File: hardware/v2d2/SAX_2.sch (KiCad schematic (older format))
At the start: 80 parts, among them J1 Prog port, J2 SSD1306, U1 74HC165, U2 74HC165, U3 74HC165, U4 BluePill_STM32F103C

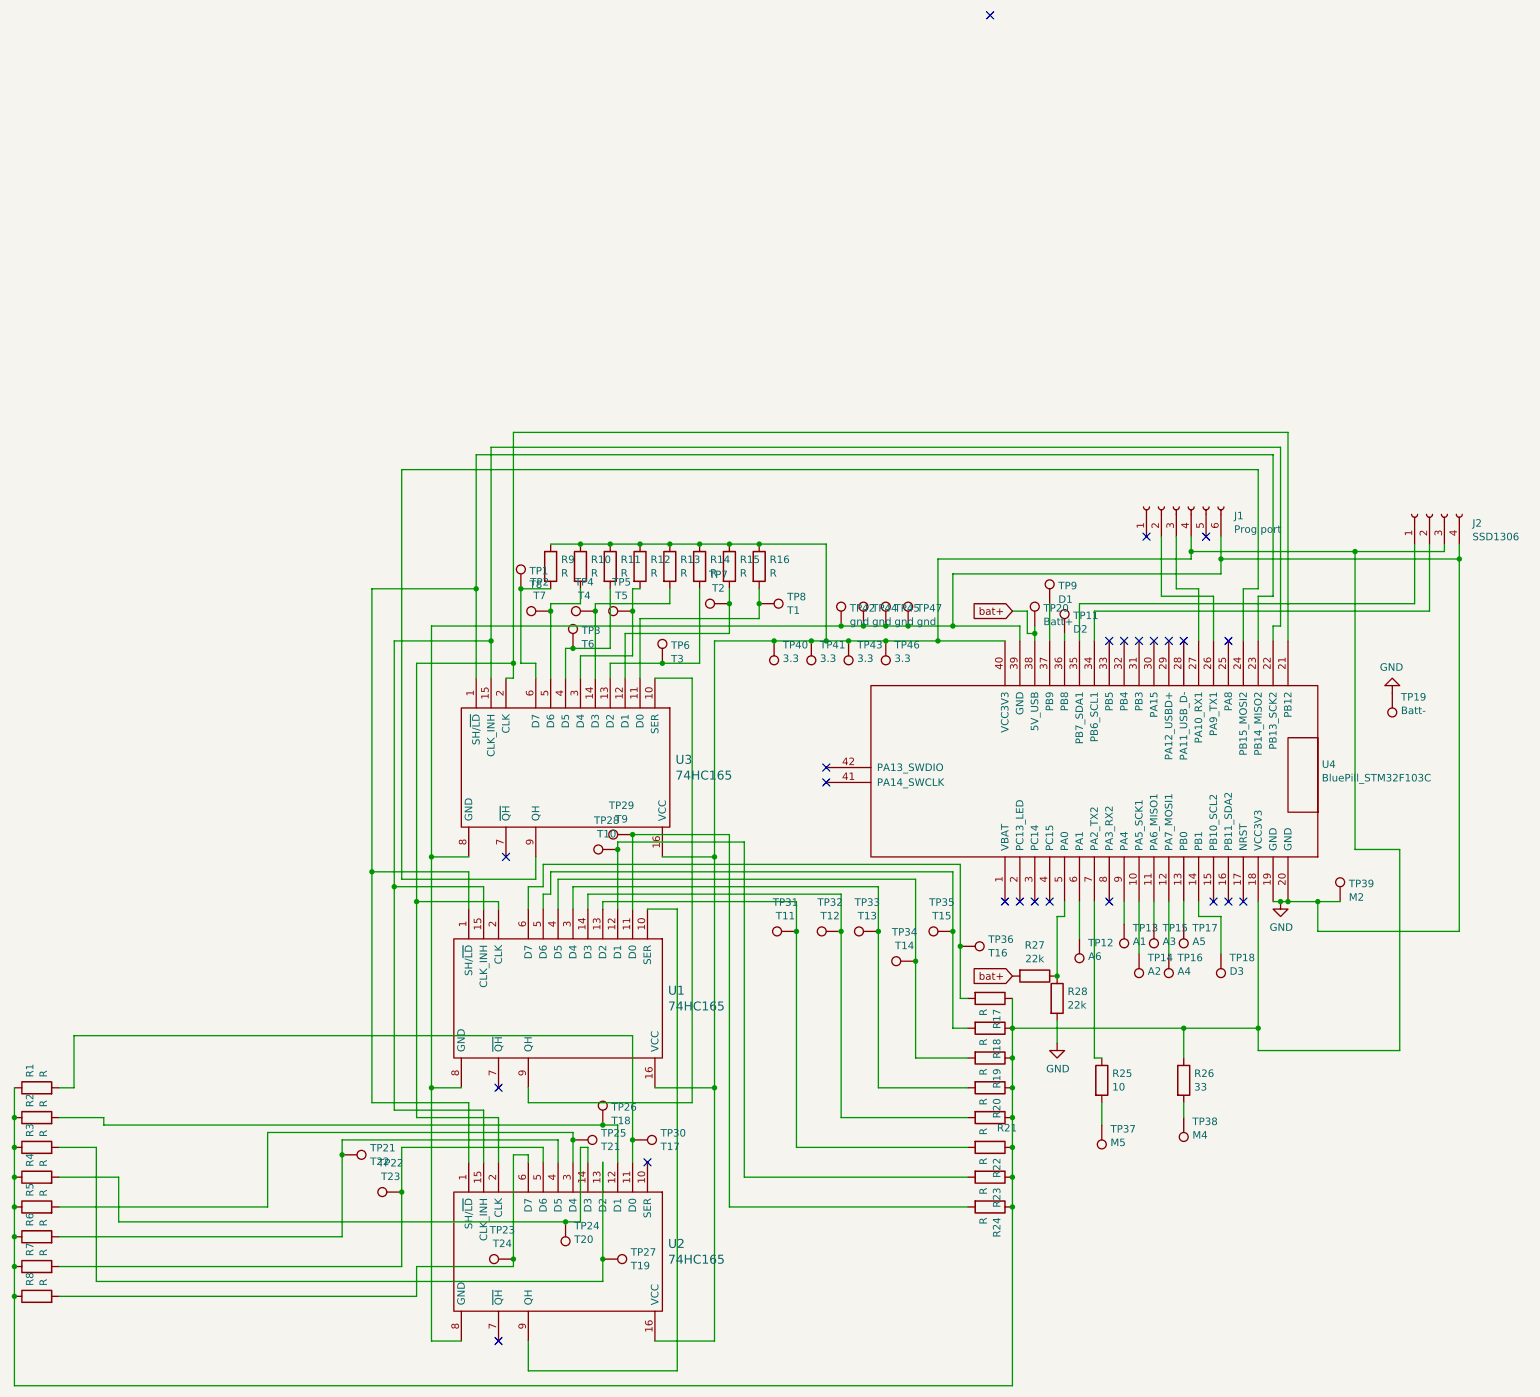
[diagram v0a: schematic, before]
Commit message: Improved fab layer
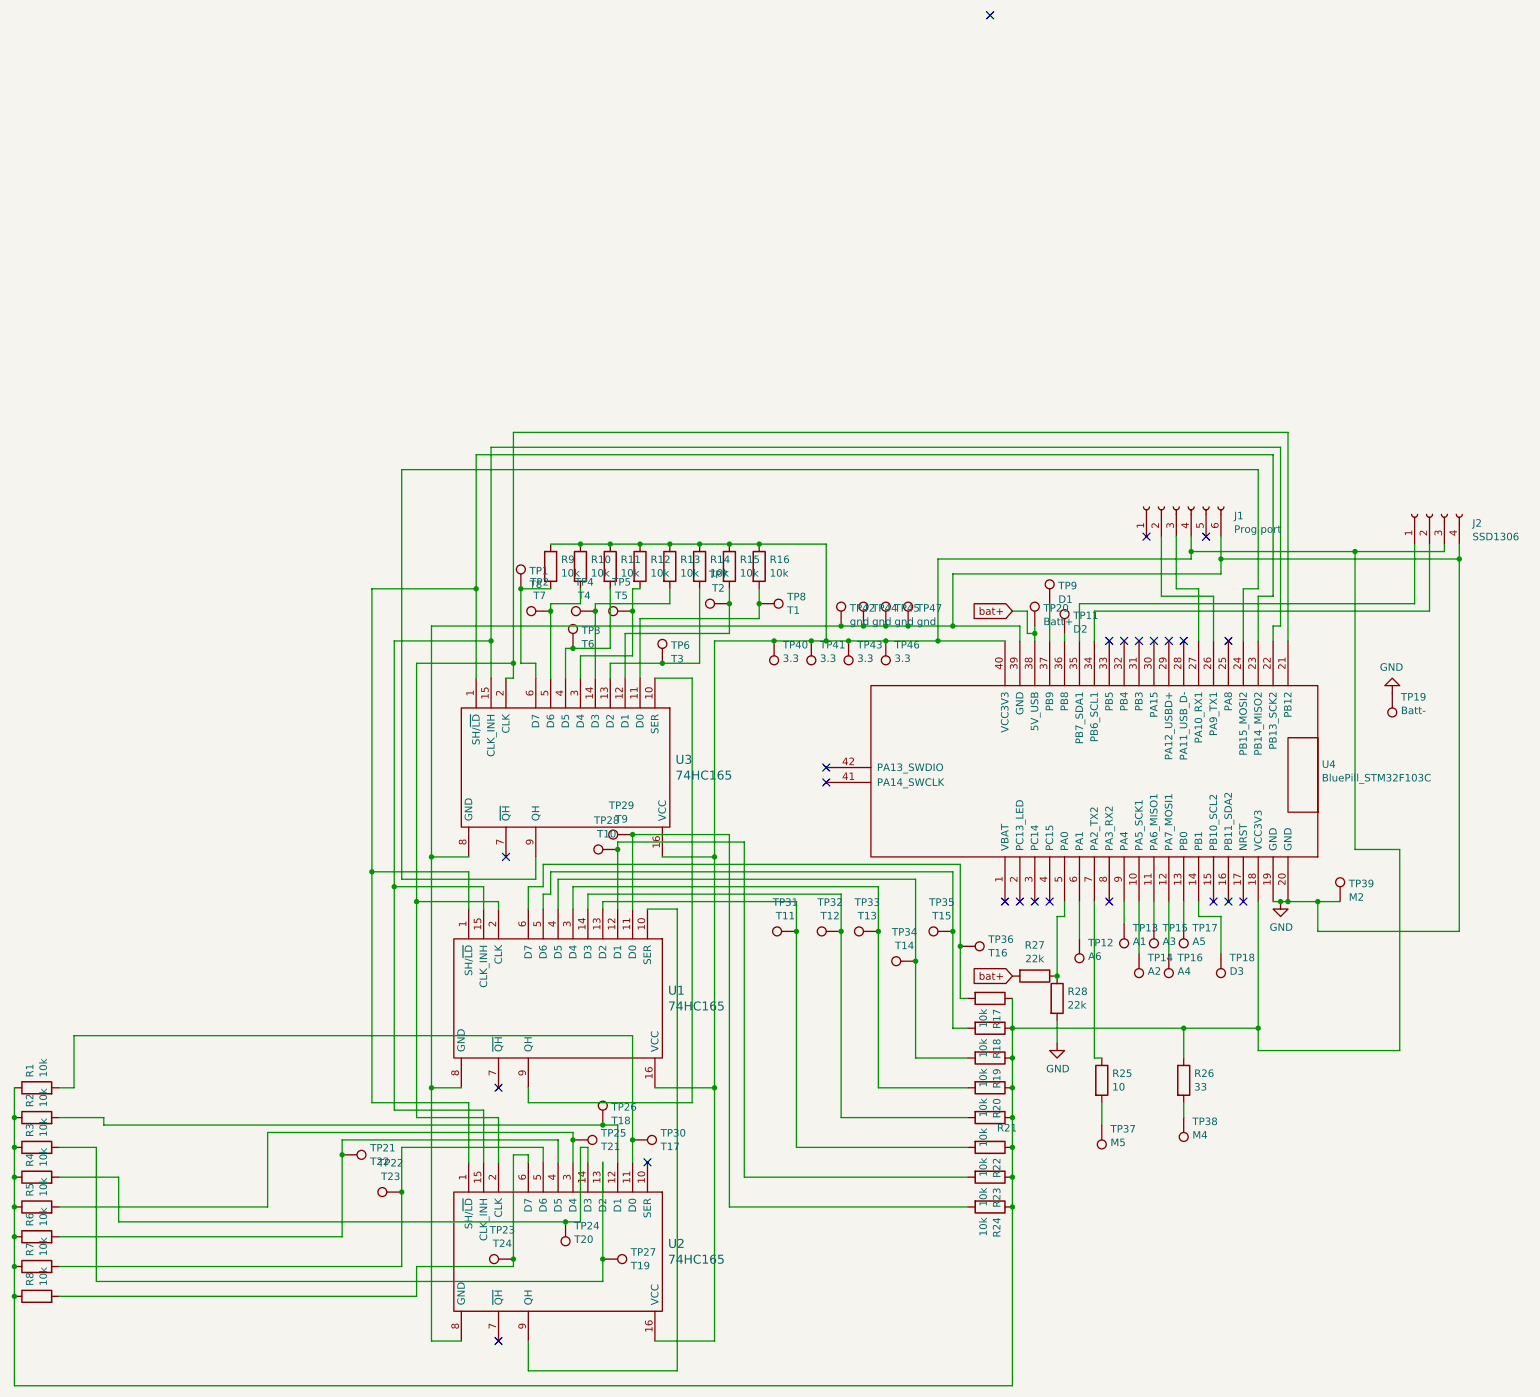
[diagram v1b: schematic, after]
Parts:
- R1, R10, R11, R12, R13, R14, R15, R16, R17, R18, R19, R2, R20, R21, R22, R23, R24, R3, R4, R5, R6, R7, R8, R9: value R -> 10k
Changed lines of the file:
@@
 P 5500 1600
 F 0 "R12" H 5570 1646 50  0000 L CNN
-F 1 "R" H 5570 1555 50  0000 L CNN
+F 1 "10k" H 5570 1555 50  0000 L CNN
 F 2 "Resistor_THT:R_Axial_DIN0207_L6.3mm_D2.5mm_P7.62mm_Horizontal" V 5430 1600 50  0001 C CNN
 F 3 "~" H 5500 1600 50  0001 C CNN
@@
 P 5300 1600
 F 0 "R11" H 5370 1646 50  0000 L CNN
-F 1 "R" H 5370 1555 50  0000 L CNN
+F 1 "10k" H 5370 1555 50  0000 L CNN
 F 2 "Resistor_THT:R_Axial_DIN0207_L6.3mm_D2.5mm_P7.62mm_Horizontal" V 5230 1600 50  0001 C CNN
 F 3 "~" H 5300 1600 50  0001 C CNN
@@
 P 5100 1600
 F 0 "R10" H 5170 1646 50  0000 L CNN
-F 1 "R" H 5170 1555 50  0000 L CNN
+F 1 "10k" H 5170 1555 50  0000 L CNN
 F 2 "Resistor_THT:R_Axial_DIN0207_L6.3mm_D2.5mm_P7.62mm_Horizontal" V 5030 1600 50  0001 C CNN
 F 3 "~" H 5100 1600 50  0001 C CNN
@@
 P 4900 1600
 F 0 "R9" H 4970 1646 50  0000 L CNN
-F 1 "R" H 4970 1555 50  0000 L CNN
+F 1 "10k" H 4970 1555 50  0000 L CNN
 F 2 "Resistor_THT:R_Axial_DIN0207_L6.3mm_D2.5mm_P7.62mm_Horizontal" V 4830 1600 50  0001 C CNN
 F 3 "~" H 4900 1600 50  0001 C CNN
@@
 P 5900 1600
 F 0 "R14" H 5970 1646 50  0000 L CNN
-F 1 "R" H 5970 1555 50  0000 L CNN
+F 1 "10k" H 5970 1555 50  0000 L CNN
 F 2 "Resistor_THT:R_Axial_DIN0207_L6.3mm_D2.5mm_P7.62mm_Horizontal" V 5830 1600 50  0001 C CNN
 F 3 "~" H 5900 1600 50  0001 C CNN
@@
 P 5700 1600
 F 0 "R13" H 5770 1646 50  0000 L CNN
-F 1 "R" H 5770 1555 50  0000 L CNN
+F 1 "10k" H 5770 1555 50  0000 L CNN
 F 2 "Resistor_THT:R_Axial_DIN0207_L6.3mm_D2.5mm_P7.62mm_Horizontal" V 5630 1600 50  0001 C CNN
 F 3 "~" H 5700 1600 50  0001 C CNN
@@
 P 6300 1600
 F 0 "R16" H 6370 1646 50  0000 L CNN
-F 1 "R" H 6370 1555 50  0000 L CNN
+F 1 "10k" H 6370 1555 50  0000 L CNN
 F 2 "Resistor_THT:R_Axial_DIN0207_L6.3mm_D2.5mm_P7.62mm_Horizontal" V 6230 1600 50  0001 C CNN
 F 3 "~" H 6300 1600 50  0001 C CNN
@@
 P 6100 1600
 F 0 "R15" H 6170 1646 50  0000 L CNN
-F 1 "R" H 6170 1555 50  0000 L CNN
+F 1 "10k" H 6170 1555 50  0000 L CNN
 F 2 "Resistor_THT:R_Axial_DIN0207_L6.3mm_D2.5mm_P7.62mm_Horizontal" V 6030 1600 50  0001 C CNN
 F 3 "~" H 6100 1600 50  0001 C CNN
@@
 P 7850 5100
 F 0 "R20" H 7920 5146 50  0000 L CNN
-F 1 "R" H 7920 5055 50  0000 L CNN
+F 1 "10k" H 7920 5055 50  0000 L CNN
 F 2 "Resistor_THT:R_Axial_DIN0207_L6.3mm_D2.5mm_P7.62mm_Horizontal" V 7780 5100 50  0001 C CNN
 F 3 "~" H 7850 5100 50  0001 C CNN
@@
 P 7850 4900
 F 0 "R19" H 7920 4946 50  0000 L CNN
-F 1 "R" H 7920 4855 50  0000 L CNN
+F 1 "10k" H 7920 4855 50  0000 L CNN
 F 2 "Resistor_THT:R_Axial_DIN0207_L6.3mm_D2.5mm_P7.62mm_Horizontal" V 7780 4900 50  0001 C CNN
 F 3 "~" H 7850 4900 50  0001 C CNN
@@
 P 7850 4700
 F 0 "R18" H 7920 4746 50  0000 L CNN
-F 1 "R" H 7920 4655 50  0000 L CNN
+F 1 "10k" H 7920 4655 50  0000 L CNN
 F 2 "Resistor_THT:R_Axial_DIN0207_L6.3mm_D2.5mm_P7.62mm_Horizontal" V 7780 4700 50  0001 C CNN
 F 3 "~" H 7850 4700 50  0001 C CNN
@@
 P 7850 4500
 F 0 "R17" H 7920 4546 50  0000 L CNN
-F 1 "R" H 7920 4455 50  0000 L CNN
+F 1 "10k" H 7920 4455 50  0000 L CNN
 F 2 "Resistor_THT:R_Axial_DIN0207_L6.3mm_D2.5mm_P7.62mm_Horizontal" V 7780 4500 50  0001 C CNN
 F 3 "~" H 7850 4500 50  0001 C CNN
@@
 P 7850 5500
 F 0 "R22" H 7920 5546 50  0000 L CNN
-F 1 "R" H 7920 5455 50  0000 L CNN
+F 1 "10k" H 7920 5455 50  0000 L CNN
 F 2 "Resistor_THT:R_Axial_DIN0207_L6.3mm_D2.5mm_P7.62mm_Horizontal" V 7780 5500 50  0001 C CNN
 F 3 "~" H 7850 5500 50  0001 C CNN
@@
 P 7850 5300
 F 0 "R21" V 7920 5346 50  0000 L CNN
-F 1 "R" H 7920 5255 50  0000 L CNN
+F 1 "10k" H 7920 5255 50  0000 L CNN
 F 2 "Resistor_THT:R_Axial_DIN0207_L6.3mm_D2.5mm_P7.62mm_Horizontal" V 7780 5300 50  0001 C CNN
 F 3 "~" H 7850 5300 50  0001 C CNN
@@
 P 7850 5900
 F 0 "R24" H 7920 5946 50  0000 L CNN
-F 1 "R" H 7920 5855 50  0000 L CNN
+F 1 "10k" H 7920 5855 50  0000 L CNN
 F 2 "Resistor_THT:R_Axial_DIN0207_L6.3mm_D2.5mm_P7.62mm_Horizontal" V 7780 5900 50  0001 C CNN
 F 3 "~" H 7850 5900 50  0001 C CNN
@@
 P 7850 5700
 F 0 "R23" H 7920 5746 50  0000 L CNN
-F 1 "R" H 7920 5655 50  0000 L CNN
+F 1 "10k" H 7920 5655 50  0000 L CNN
 F 2 "Resistor_THT:R_Axial_DIN0207_L6.3mm_D2.5mm_P7.62mm_Horizontal" V 7780 5700 50  0001 C CNN
 F 3 "~" H 7850 5700 50  0001 C CNN
@@
 P 1450 5900
 F 0 "R5" H 1520 5946 50  0000 L CNN
-F 1 "R" H 1520 5855 50  0000 L CNN
+F 1 "10k" H 1520 5855 50  0000 L CNN
 F 2 "Resistor_THT:R_Axial_DIN0207_L6.3mm_D2.5mm_P7.62mm_Horizontal" V 1380 5900 50  0001 C CNN
 F 3 "~" H 1450 5900 50  0001 C CNN
@@
 P 1450 6100
 F 0 "R6" H 1520 6146 50  0000 L CNN
-F 1 "R" H 1520 6055 50  0000 L CNN
+F 1 "10k" H 1520 6055 50  0000 L CNN
 F 2 "Resistor_THT:R_Axial_DIN0207_L6.3mm_D2.5mm_P7.62mm_Horizontal" V 1380 6100 50  0001 C CNN
 F 3 "~" H 1450 6100 50  0001 C CNN
@@
 P 1450 6300
 F 0 "R7" H 1520 6346 50  0000 L CNN
-F 1 "R" H 1520 6255 50  0000 L CNN
+F 1 "10k" H 1520 6255 50  0000 L CNN
 F 2 "Resistor_THT:R_Axial_DIN0207_L6.3mm_D2.5mm_P7.62mm_Horizontal" V 1380 6300 50  0001 C CNN
 F 3 "~" H 1450 6300 50  0001 C CNN
@@
 P 1450 6500
 F 0 "R8" H 1520 6546 50  0000 L CNN
-F 1 "R" H 1520 6455 50  0000 L CNN
+F 1 "10k" H 1520 6455 50  0000 L CNN
 F 2 "Resistor_THT:R_Axial_DIN0207_L6.3mm_D2.5mm_P7.62mm_Horizontal" V 1380 6500 50  0001 C CNN
 F 3 "~" H 1450 6500 50  0001 C CNN
@@
 P 1450 5500
 F 0 "R3" H 1520 5546 50  0000 L CNN
-F 1 "R" H 1520 5455 50  0000 L CNN
+F 1 "10k" H 1520 5455 50  0000 L CNN
 F 2 "Resistor_THT:R_Axial_DIN0207_L6.3mm_D2.5mm_P7.62mm_Horizontal" V 1380 5500 50  0001 C CNN
 F 3 "~" H 1450 5500 50  0001 C CNN
@@
 P 1450 5700
 F 0 "R4" H 1520 5746 50  0000 L CNN
-F 1 "R" H 1520 5655 50  0000 L CNN
+F 1 "10k" H 1520 5655 50  0000 L CNN
 F 2 "Resistor_THT:R_Axial_DIN0207_L6.3mm_D2.5mm_P7.62mm_Horizontal" V 1380 5700 50  0001 C CNN
 F 3 "~" H 1450 5700 50  0001 C CNN
@@
 P 1450 5100
 F 0 "R1" H 1520 5146 50  0000 L CNN
-F 1 "R" H 1520 5055 50  0000 L CNN
+F 1 "10k" H 1520 5055 50  0000 L CNN
 F 2 "Resistor_THT:R_Axial_DIN0207_L6.3mm_D2.5mm_P7.62mm_Horizontal" V 1380 5100 50  0001 C CNN
 F 3 "~" H 1450 5100 50  0001 C CNN
@@
 P 1450 5300
 F 0 "R2" H 1520 5346 50  0000 L CNN
-F 1 "R" H 1520 5255 50  0000 L CNN
+F 1 "10k" H 1520 5255 50  0000 L CNN
 F 2 "Resistor_THT:R_Axial_DIN0207_L6.3mm_D2.5mm_P7.62mm_Horizontal" V 1380 5300 50  0001 C CNN
 F 3 "~" H 1450 5300 50  0001 C CNN
